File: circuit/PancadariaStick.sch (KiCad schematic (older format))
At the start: 17 parts, among them CON1 AVR-ISP-10, IC1 ATMEGA8-P, P1 Joystick, P2 Buttons, P3 USB type B, Q1 16MHz

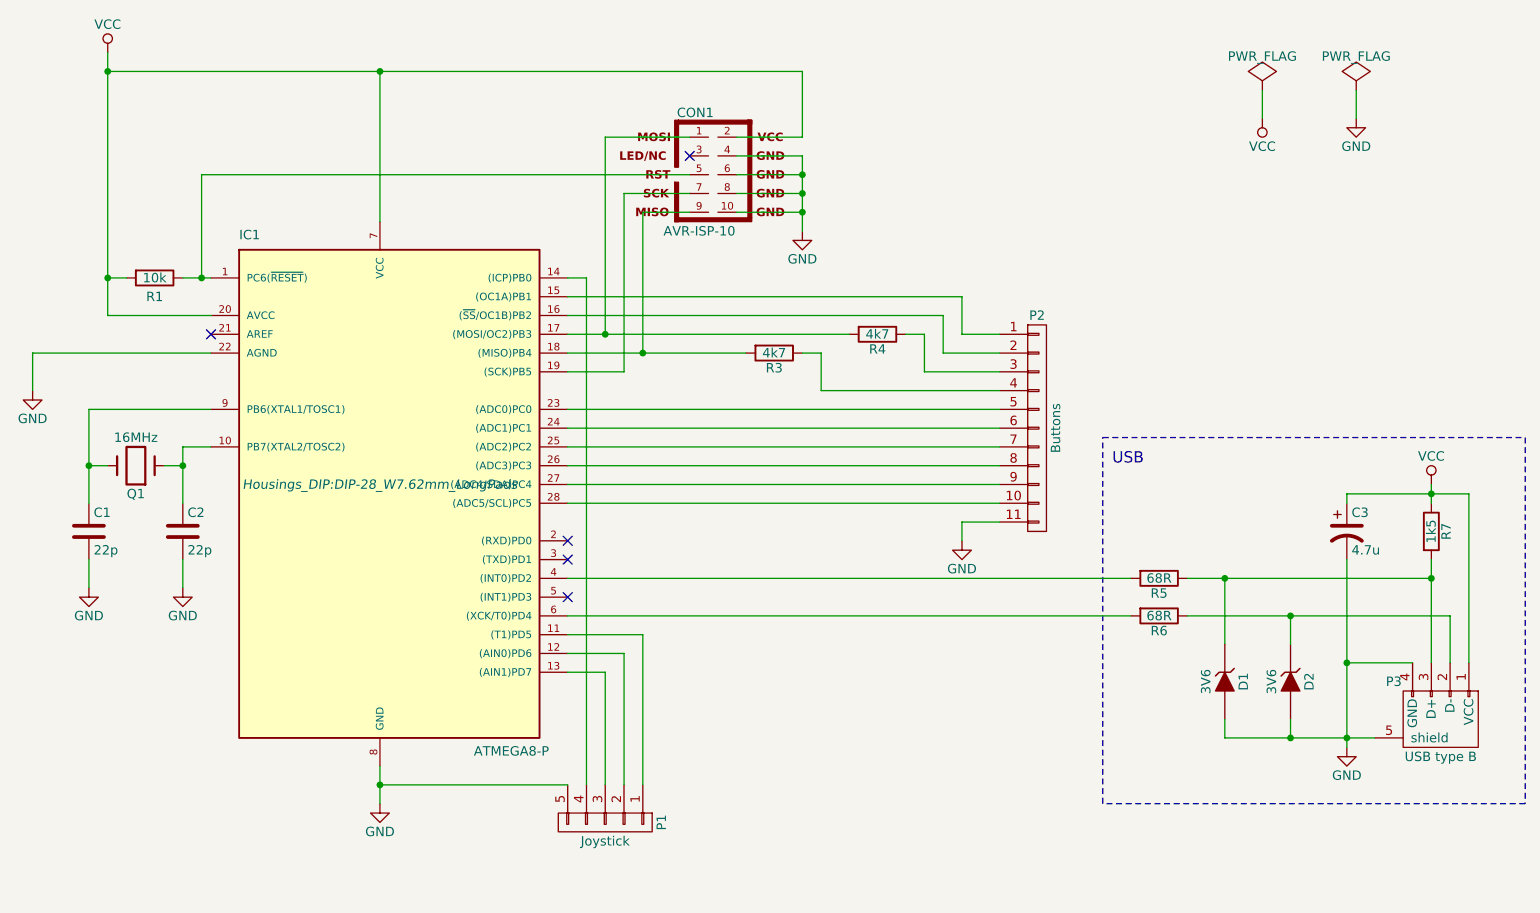
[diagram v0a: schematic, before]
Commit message: Updated board, removed ISP header, changed connectors to block terminals, added LED. Added plots.
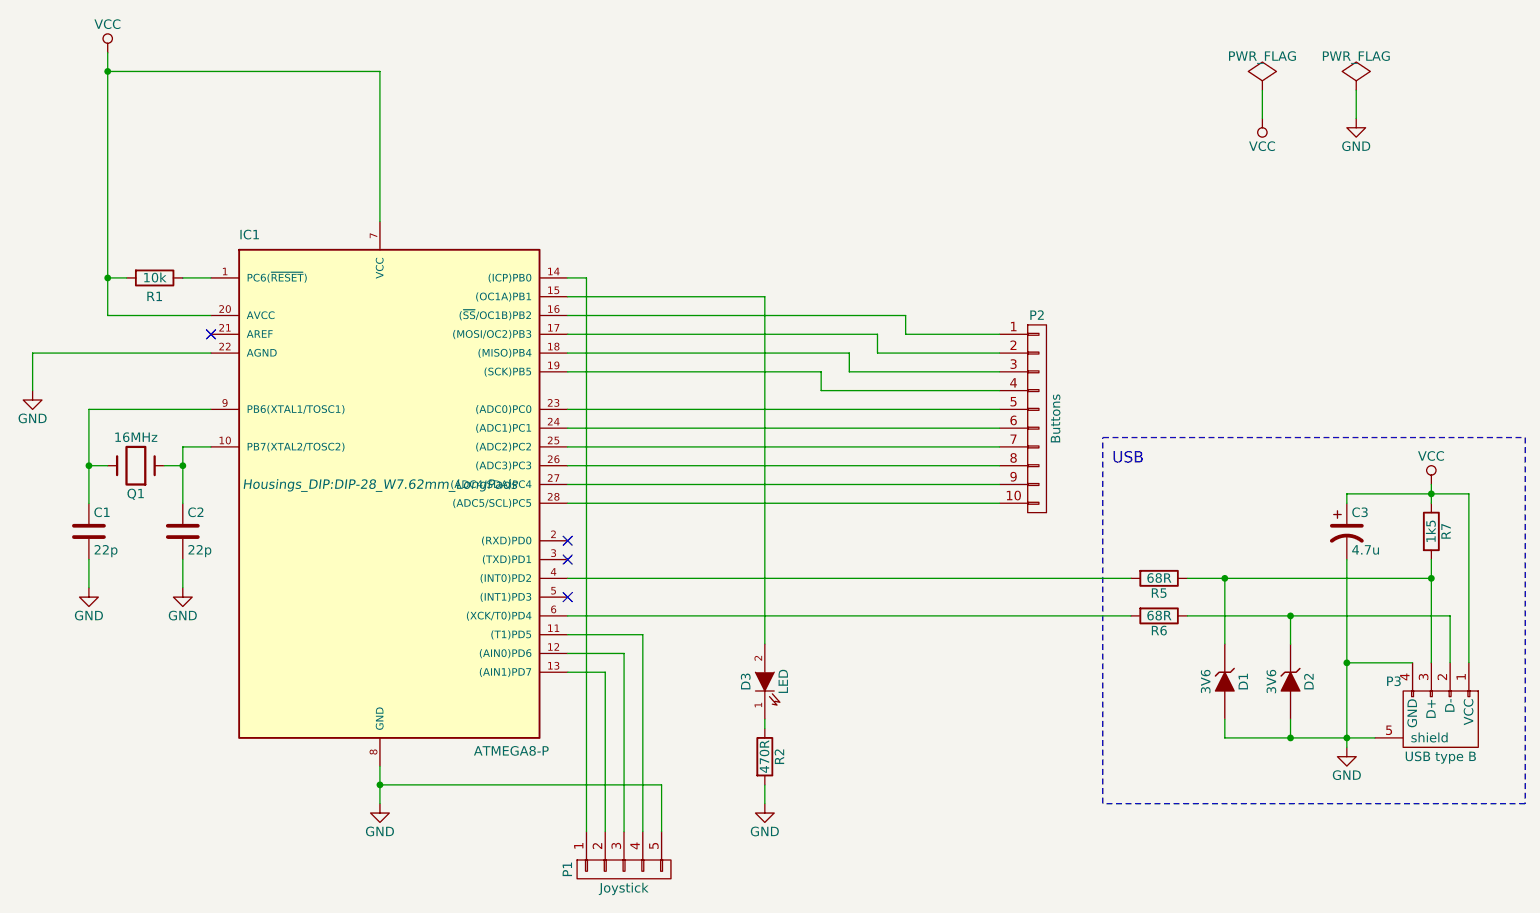
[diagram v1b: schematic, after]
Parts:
- removed CON1: AVR-ISP-10, Connect:IDC_Header_Straight_10pins, symbol AVR-ISP-10
- removed P2: Buttons, Pin_Headers:Pin_Header_Straight_1x11, symbol CONN_01X11
- removed R3, R4: 4k7, Resistors_ThroughHole:Resistor_Horizontal_RM7mm, symbol R
- added D?: LED, symbol LED
- added P2: Buttons, Terminal_Blocks:TerminalBlock_Pheonix_MKDS1.5-10pol, symbol CONN_01X10
- added R?: 470R, symbol R
- P1: footprint Pin_Headers:Pin_Header_Straight_1x05 -> Terminal_Blocks:TerminalBlock_Pheonix_MKDS1.5-5pol
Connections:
- net GND: now also R?.2
- net at IC1.11 ((T1)PD5): now also P1.4 (P4); no longer P1.1 (P1)
- net at IC1.12 ((AIN0)PD6): now also P1.3 (P3); no longer P1.2 (P2)
- net at IC1.13 ((AIN1)PD7): now also P1.2 (P2); no longer P1.3 (P3)
- net at IC1.14 ((ICP)PB0): now also P1.1 (P1); no longer P1.4 (P4)
- net at IC1.15 ((OC1A)PB1): now also D?.2 (A)
- net at IC1.16 ((~SS~/OC1B)PB2): now also P2.1 (P1)
- net at IC1.17 ((MOSI/OC2)PB3): now also P2.2 (P2)
- net at IC1.18 ((MISO)PB4): now also P2.3 (P3)
- net at IC1.19 ((SCK)PB5): now also P2.4 (P4)
- net at IC1.23 ((ADC0)PC0): now also P2.5 (P5)
- net at IC1.24 ((ADC1)PC1): now also P2.6 (P6)
- net at IC1.25 ((ADC2)PC2): now also P2.7 (P7)
- net at IC1.26 ((ADC3)PC3): now also P2.8 (P8)
- net at IC1.27 ((ADC4/SDA)PC4): now also P2.9 (P9)
- net at IC1.28 ((ADC5/SCL)PC5): now also P2.10 (P10)
- new net: D?.1 (K), R?.1
- no-connect marks 5 -> 4
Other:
- moved on the sheet: P1
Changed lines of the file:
@@
-$EndComp
-$Comp
-L R R4
-U 1 1 57AE0D01
-P 5550 2600
-F 0 "R4" V 5630 2600 50  0000 C CNN
-F 1 "4k7" V 5550 2600 50  0000 C CNN
-F 2 "Resistors_ThroughHole:Resistor_Horizontal_RM7mm" V 5480 2600 50  0001 C CNN
-F 3 "" H 5550 2600 50  0000 C CNN
-	1    5550 2600
-	0    1    1    0
 $EndComp
 $Comp
@@
 $EndComp
 $Comp
-L GND #PWR08
-U 1 1 57AE3D29
-P 5150 2050
-F 0 "#PWR08" H 5150 1800 50  0001 C CNN
-F 1 "GND" H 5150 1900 50  0000 C CNN
-F 2 "" H 5150 2050 50  0000 C CNN
-F 3 "" H 5150 2050 50  0000 C CNN
-	1    5150 2050
-	1    0    0    -1
-$EndComp
-$Comp
 L CP1 C3
 U 1 1 57AE3E46
@@
 	1    0    0    -1
 $EndComp
-$Comp
-L R R3
-U 1 1 57AE44A8
-P 5000 2700
-F 0 "R3" V 5080 2700 50  0000 C CNN
-F 1 "4k7" V 5000 2700 50  0000 C CNN
-F 2 "Resistors_ThroughHole:Resistor_Horizontal_RM7mm" V 4930 2700 50  0001 C CNN
-F 3 "" H 5000 2700 50  0000 C CNN
-	1    5000 2700
-	0    1    1    0
-$EndComp
 NoConn ~ 2000 2600
 $Comp
 L CONN_01X05 P1
 U 1 1 57AE4D3E
-P 4100 5200
-F 0 "P1" H 4100 5500 50  0000 C CNN
-F 1 "Joystick" V 4200 5200 50  0000 C CNN
-F 2 "Pin_Headers:Pin_Header_Straight_1x05" H 4100 5200 50  0001 C CNN
-F 3 "" H 4100 5200 50  0000 C CNN
-	1    4100 5200
-	0    1    1    0
-$EndComp
-$Comp
-L CONN_01X11 P2
-U 1 1 57AE6DF7
-P 6400 3100
-F 0 "P2" H 6400 3700 50  0000 C CNN
-F 1 "Buttons" V 6500 3100 50  0000 C CNN
-F 2 "Pin_Headers:Pin_Header_Straight_1x11" H 6400 3100 50  0001 C CNN
-F 3 "" H 6400 3100 50  0000 C CNN
-	1    6400 3100
-	1    0    0    -1
-$EndComp
-$Comp
-L GND #PWR09
-U 1 1 57AE79F2
-P 6000 3700
-F 0 "#PWR09" H 6000 3450 50  0001 C CNN
-F 1 "GND" H 6000 3550 50  0000 C CNN
-F 2 "" H 6000 3700 50  0000 C CNN
-F 3 "" H 6000 3700 50  0000 C CNN
-	1    6000 3700
-	1    0    0    -1
+P 4200 5450
+F 0 "P1" H 4200 5750 50  0000 C CNN
+F 1 "Joystick" V 4300 5450 50  0000 C CNN
+F 2 "Terminal_Blocks:TerminalBlock_Pheonix_MKDS1.5-5pol" H 4200 5450 50  0001 C CNN
+F 3 "" H 4200 5450 50  0000 C CNN
+	1    4200 5450
+	0    -1   1    0
 $EndComp
 NoConn ~ 3900 3700
@@
 USB
 $Comp
-L PWR_FLAG #FLG010
+L PWR_FLAG #FLG08
 U 1 1 57AE89A3
 P 7600 1300
-F 0 "#FLG010" H 7600 1395 50  0001 C CNN
+F 0 "#FLG08" H 7600 1395 50  0001 C CNN
 F 1 "PWR_FLAG" H 7600 1480 50  0000 C CNN
 F 2 "" H 7600 1300 50  0000 C CNN
@@
 $EndComp
 $Comp
-L VCC #PWR011
+L VCC #PWR09
 U 1 1 57AE89ED
 P 7600 1450
-F 0 "#PWR011" H 7600 1300 50  0001 C CNN
+F 0 "#PWR09" H 7600 1300 50  0001 C CNN
 F 1 "VCC" H 7600 1600 50  0000 C CNN
 F 2 "" H 7600 1450 50  0000 C CNN
@@
 $EndComp
 $Comp
-L PWR_FLAG #FLG012
+L PWR_FLAG #FLG010
 U 1 1 57AE8A35
 P 8100 1300
-F 0 "#FLG012" H 8100 1395 50  0001 C CNN
+F 0 "#FLG010" H 8100 1395 50  0001 C CNN
 F 1 "PWR_FLAG" H 8100 1480 50  0000 C CNN
 F 2 "" H 8100 1300 50  0000 C CNN
@@
 $EndComp
 $Comp
-L GND #PWR013
+L GND #PWR011
 U 1 1 57AE8A76
 P 8100 1450
-F 0 "#PWR013" H 8100 1200 50  0001 C CNN
+F 0 "#PWR011" H 8100 1200 50  0001 C CNN
 F 1 "GND" H 8100 1300 50  0000 C CNN
 F 2 "" H 8100 1450 50  0000 C CNN
@@
 $EndComp
 $Comp
-L AVR-ISP-10 CON1
-U 1 1 57B1FDDF
-P 4750 1750
-F 0 "CON1" H 4580 2080 50  0000 C CNN
-F 1 "AVR-ISP-10" H 4410 1420 50  0000 L BNN
-F 2 "Connect:IDC_Header_Straight_10pins" V 4000 1800 50  0001 C CNN
-F 3 "" H 4750 1750 50  0000 C CNN
-	1    4750 1750
-	1    0    0    -1
-$EndComp
-NoConn ~ 4550 1650
-Wire Wire Line
-	1850 2300 2000 2300
+L CONN_01X10 P2
+U 1 1 5822F490
+P 6400 3050
+F 0 "P2" H 6400 3600 50  0000 C CNN
+F 1 "Buttons" V 6500 3050 50  0000 C CNN
+F 2 "Terminal_Blocks:TerminalBlock_Pheonix_MKDS1.5-10pol" H 6400 3050 50  0001 C CNN
+F 3 "" H 6400 3050 50  0000 C CNN
+	1    6400 3050
+	1    0    0    -1
+$EndComp
 Wire Wire Line
 	1450 2300 1550 2300
@@
 	1050 2700 1050 2900
 Wire Wire Line
-	2900 4900 2900 5100
-Wire Wire Line
 	1450 2500 2000 2500
 Wire Wire Line
@@
 Connection ~ 8500 3450
 Wire Wire Line
-	1950 1750 1950 2300
-Connection ~ 1950 2300
-Wire Wire Line
 	8050 3450 8050 3500
 Connection ~ 8050 4350
-Connection ~ 2900 5000
 Wire Wire Line
 	3900 2300 4000 2300
 Wire Wire Line
-	4000 2300 4000 5000
-Wire Wire Line
-	3900 5000 2900 5000
-Wire Wire Line
 	3900 4300 4200 4300
 Wire Wire Line
-	4200 4300 4200 5000
-Wire Wire Line
 	3900 3100 6200 3100
 Wire Wire Line
@@
 Wire Wire Line
 	3900 3500 6200 3500
-Wire Wire Line
-	5150 2700 5250 2700
-Wire Wire Line
-	5250 2700 5250 2900
-Wire Wire Line
-	5700 2600 5800 2600
-Wire Wire Line
-	5800 2600 5800 2800
-Wire Wire Line
-	3900 2500 5900 2500
-Wire Wire Line
-	5900 2500 5900 2700
 Wire Notes Line
 	9000 3150 9000 5100
@@
 	6900 4100 3900 4100
 Wire Wire Line
-	6200 3600 6000 3600
-Wire Wire Line
-	6000 3600 6000 3700
-Wire Wire Line
 	7600 1300 7600 1450
 Wire Wire Line
 	8100 1300 8100 1450
-Wire Wire Line
-	3900 2600 5400 2600
-Wire Wire Line
-	5150 1950 4800 1950
-Wire Wire Line
-	5150 1850 4800 1850
-Wire Wire Line
-	5150 1650 5150 2050
-Connection ~ 5150 1950
-Connection ~ 5150 1850
-Wire Wire Line
-	4800 1650 5150 1650
-Connection ~ 5150 1750
-Wire Wire Line
-	4800 1550 5150 1550
-Wire Wire Line
-	5150 1200 5150 1550
-Wire Wire Line
-	1450 1200 5150 1200
 Connection ~ 1450 1200
 Wire Wire Line
-	2900 2000 2900 1200
-Connection ~ 2900 1200
-Wire Wire Line
-	4550 1750 1950 1750
-Wire Wire Line
-	3900 2700 4850 2700
-Wire Wire Line
-	4550 1550 4100 1550
-Wire Wire Line
-	4100 1550 4100 2600
-Connection ~ 4100 2600
-Wire Wire Line
-	4550 1850 4200 1850
-Wire Wire Line
-	4550 1950 4300 1950
-Wire Wire Line
-	4300 1950 4300 2700
-Connection ~ 4300 2700
-Wire Wire Line
-	4800 1750 5150 1750
-Wire Wire Line
 	3900 4200 4300 4200
 Wire Wire Line
-	4300 4200 4300 5000
-Wire Wire Line
 	3900 4400 4100 4400
 Wire Wire Line
-	4100 4400 4100 5000
-Wire Wire Line
-	4200 1850 4200 2800
-Wire Wire Line
-	4200 2800 3900 2800
-Wire Wire Line
 	6200 3000 3900 3000
 Wire Wire Line
 	5250 2900 6200 2900
 Wire Wire Line
-	5800 2800 6200 2800
-Wire Wire Line
-	5900 2700 6200 2700
-Wire Wire Line
-	6000 2400 6000 2600
-Wire Wire Line
-	6000 2600 6200 2600
-Wire Wire Line
-	3900 2400 6000 2400
+	5700 2600 6200 2600
+Wire Wire Line
+	1450 1200 2900 1200
+Wire Wire Line
+	2900 1200 2900 2000
+Wire Wire Line
+	2000 2300 1850 2300
+Wire Wire Line
+	3900 2800 5250 2800
+Wire Wire Line
+	5250 2800 5250 2900
+Wire Wire Line
+	3900 2700 5400 2700
+Wire Wire Line
+	5400 2700 5400 2800
+Wire Wire Line
+	5400 2800 6200 2800
+Wire Wire Line
+	3900 2600 5550 2600
+Wire Wire Line
+	5550 2600 5550 2700
+Wire Wire Line
+	5550 2700 6200 2700
+Wire Wire Line
+	5700 2600 5700 2500
+Wire Wire Line
+	5700 2500 3900 2500
+Connection ~ 2900 5000
+Wire Wire Line
+	2900 4900 2900 5100
+Wire Wire Line
+	4000 2300 4000 5250
+Wire Wire Line
+	4100 4400 4100 5250
+Wire Wire Line
+	4200 4300 4200 5250
+Wire Wire Line
+	4300 4200 4300 5250
+Wire Wire Line
+	4400 5250 4400 5000
+Wire Wire Line
+	4400 5000 2900 5000
+$Comp
+L LED D?
+U 1 1 58234200
+P 4950 4450
+F 0 "D3" H 4950 4550 50  0000 C CNN
+F 1 "LED" H 4950 4350 50  0000 C CNN
+F 2 "" H 4950 4450 50  0000 C CNN
+F 3 "" H 4950 4450 50  0000 C CNN
+	1    4950 4450
+	0    -1   -1   0
+$EndComp
+$Comp
+L R R?
+U 1 1 58234267
+P 4950 4850
+F 0 "R2" V 5030 4850 50  0000 C CNN
+F 1 "470R" V 4950 4850 50  0000 C CNN
+F 2 "" V 4880 4850 50  0000 C CNN
+F 3 "" H 4950 4850 50  0000 C CNN
+	1    4950 4850
+	1    0    0    -1
+$EndComp
+$Comp
+L GND #PWR?
+U 1 1 582342D3
+P 4950 5100
+F 0 "#PWR?" H 4950 4850 50  0001 C CNN
+F 1 "GND" H 4950 4950 50  0000 C CNN
+F 2 "" H 4950 5100 50  0000 C CNN
+F 3 "" H 4950 5100 50  0000 C CNN
+	1    4950 5100
+	1    0    0    -1
+$EndComp
+Wire Wire Line
+	4950 5100 4950 5000
+Wire Wire Line
+	4950 4700 4950 4650
+Wire Wire Line
+	3900 2400 4950 2400
+Wire Wire Line
+	4950 2400 4950 4250
 $EndSCHEMATC
